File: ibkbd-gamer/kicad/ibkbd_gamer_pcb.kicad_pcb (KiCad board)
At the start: 2 copper layers, 165.6 x 144.3 mm, 35 parts

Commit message: update pcb
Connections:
- S1 pad : P5 -> P2
- S1 pad 1: P5 -> P2
- S10 pad : P7 -> ring_home
- S10 pad 1: P7 -> P4
- S10 pad 2: P16 -> P14
- S11 pad : P7 -> ring_top
- S11 pad 1: P7 -> P4
- S11 pad 2: P18 -> P16
- S12 pad : P7 -> ring_num
- S12 pad 1: P7 -> P4
- S12 pad 2: P19 -> P10
- S13 pad : P8 -> middle_bottom
- S13 pad 1: P8 -> P5
- S14 pad : P8 -> middle_home
- S14 pad 1: P8 -> P5
- S14 pad 2: P16 -> P14
- S15 pad : P8 -> middle_top
- S15 pad 1: P8 -> P5
- S15 pad 2: P18 -> P16
- S16 pad : P8 -> middle_num
- S16 pad 1: P8 -> P5
- S16 pad 2: P19 -> P10
- S17 pad : P9 -> index_bottom
- S17 pad 1: P9 -> P6
- S18 pad : P9 -> index_home
- S18 pad 1: P9 -> P6
- S18 pad 2: P16 -> P14
- S19 pad : P9 -> index_top
- S19 pad 1: P9 -> P6
- S19 pad 2: P18 -> P16
- S2 pad : P5 -> outer_home
- S2 pad 1: P5 -> P2
- S2 pad 2: P16 -> P14
- S20 pad : P9 -> P6
- S20 pad 1: P9 -> P6
- S20 pad 2: P19 -> P10
- S21 pad : P10 -> inner_bottom
- S21 pad 1: P10 -> P7
- S22 pad : P10 -> inner_home
- S22 pad 1: P10 -> P7
- S22 pad 2: P16 -> P14
- S23 pad : P10 -> inner_top
- S23 pad 1: P10 -> P7
- S23 pad 2: P18 -> P16
- S24 pad : P10 -> P7
- S24 pad 1: P10 -> P7
- S24 pad 2: P19 -> P10
- S25 pad : P14 -> extra_home
- S25 pad 1: P14 -> P8
- S25 pad 2: P16 -> P14
- S26 pad : P14 -> extra_top
- S26 pad 1: P14 -> P8
- S26 pad 2: P18 -> P16
- S27 pad : P14 -> extra_num
- S27 pad 1: P14 -> P8
- S27 pad 2: P19 -> P10
- S28 pad : P9 -> P6
- S28 pad 1: P9 -> P6
- S28 pad 2: P20 -> P18
- S29 pad : P10 -> home_thumb
- S29 pad 1: P10 -> P7
- S29 pad 2: P20 -> P18
- S3 pad : P5 -> outer_top
- S3 pad 1: P5 -> P2
- S3 pad 2: P18 -> P16
- S30 pad : P10 -> far_thumb
- S30 pad 1: P10 -> P7
- S30 pad 2: P21 -> P19
- S31 pad : P14 -> gk1_thumb
- S31 pad 1: P14 -> P8
- S31 pad 2: P20 -> P18
- S32 pad : P14 -> gk2_thumb
- S32 pad 1: P14 -> P8
- S33 pad : P14 -> P8
- S33 pad 1: P14 -> P8
- S33 pad 2: P21 -> P19
- S4 pad : P5 -> outer_num
- S4 pad 1: P5 -> P2
- S4 pad 2: P19 -> P10
- S5 pad : P6 -> P3
- S5 pad 1: P6 -> P3
- S6 pad : P6 -> pinky_home
- S6 pad 1: P6 -> P3
- S6 pad 2: P16 -> P14
- S7 pad : P6 -> P3
- S7 pad 1: P6 -> P3
- S7 pad 2: P18 -> P16
- S8 pad : P6 -> P3
- S8 pad 1: P6 -> P3
- S8 pad 2: P19 -> P10
- S9 pad : P7 -> ring_bottom
- S9 pad 1: P7 -> P4
- TRRS1 pad 3: P4 -> P9
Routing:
- net P19: track 0.00 -> 272.1 mm
- net P8: track 63.2 -> 328.2 mm
- net (no net): track 262.1 -> 0.00 mm
- net P18: track 0.00 -> 254.6 mm
- net P15: track 0.00 -> 250.1 mm
- net P7: track 63.2 -> 306.6 mm
- net P16: track 0.00 -> 194.4 mm
- net P6: track 63.2 -> 247.4 mm
- net GND: track 0.00 -> 169.9 mm
- net P4: track 0.00 -> 168.2 mm
- net P3: track 0.00 -> 154.6 mm
- net P2: track 0.00 -> 147.1 mm
- net VCC: track 0.00 -> 135.6 mm
- net P14: track 94.9 -> 228.2 mm
- net P5: track 63.2 -> 187.3 mm
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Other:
- net class Default removed

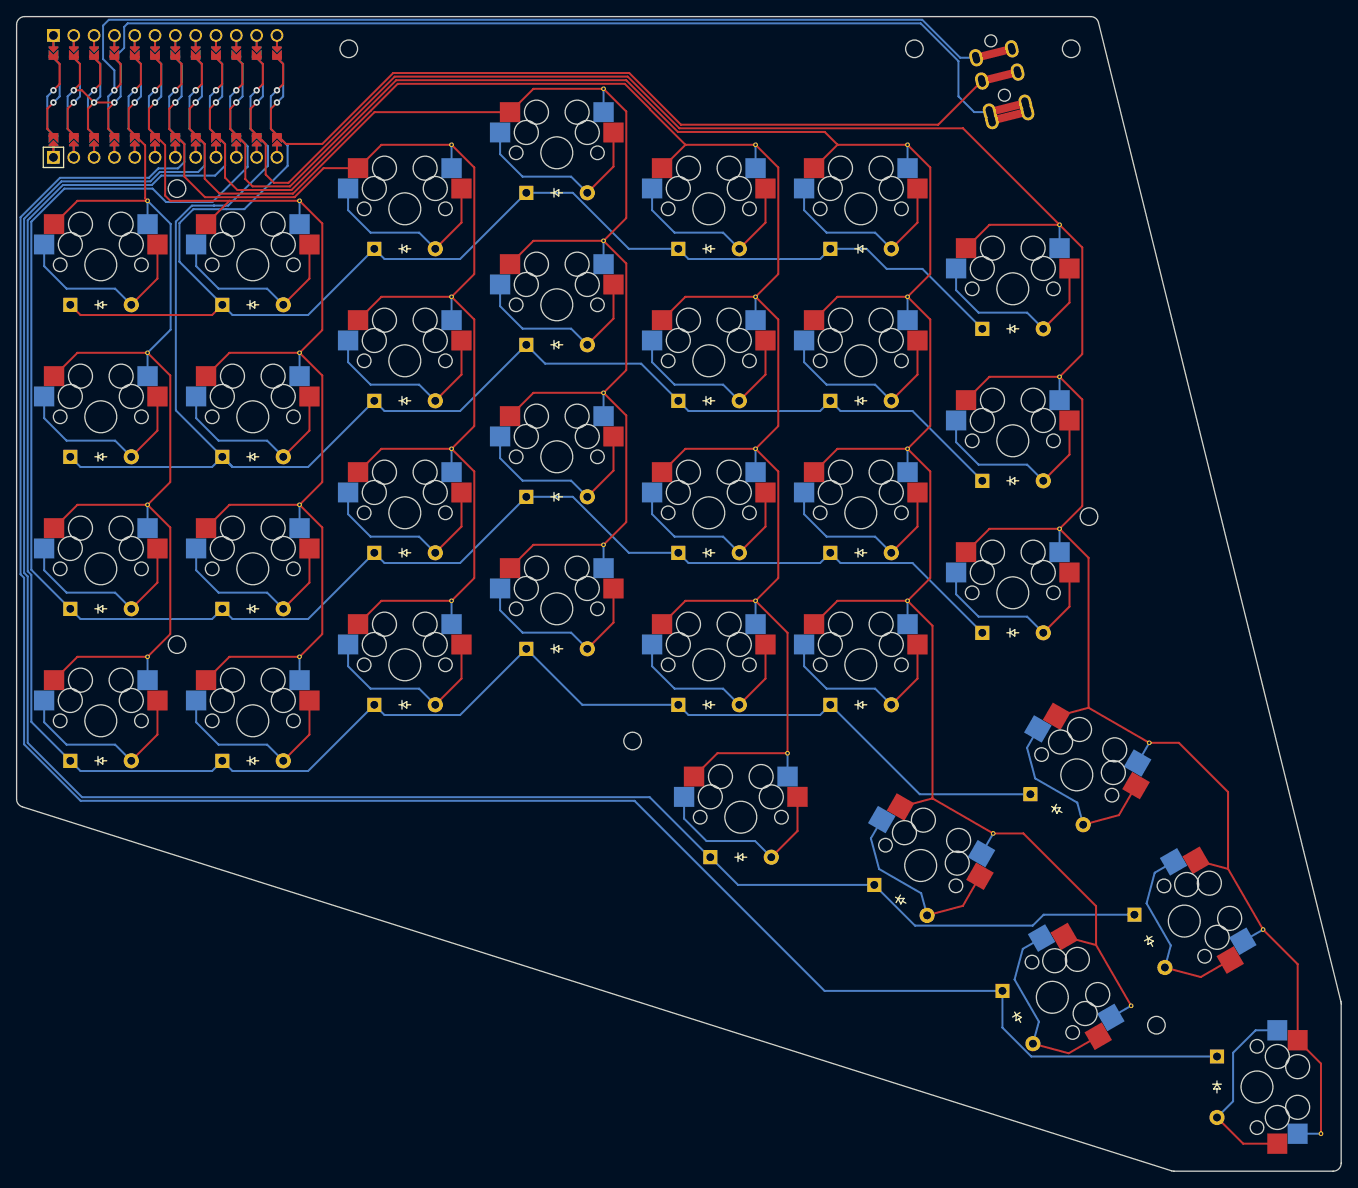
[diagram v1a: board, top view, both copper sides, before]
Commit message: move to through hole design
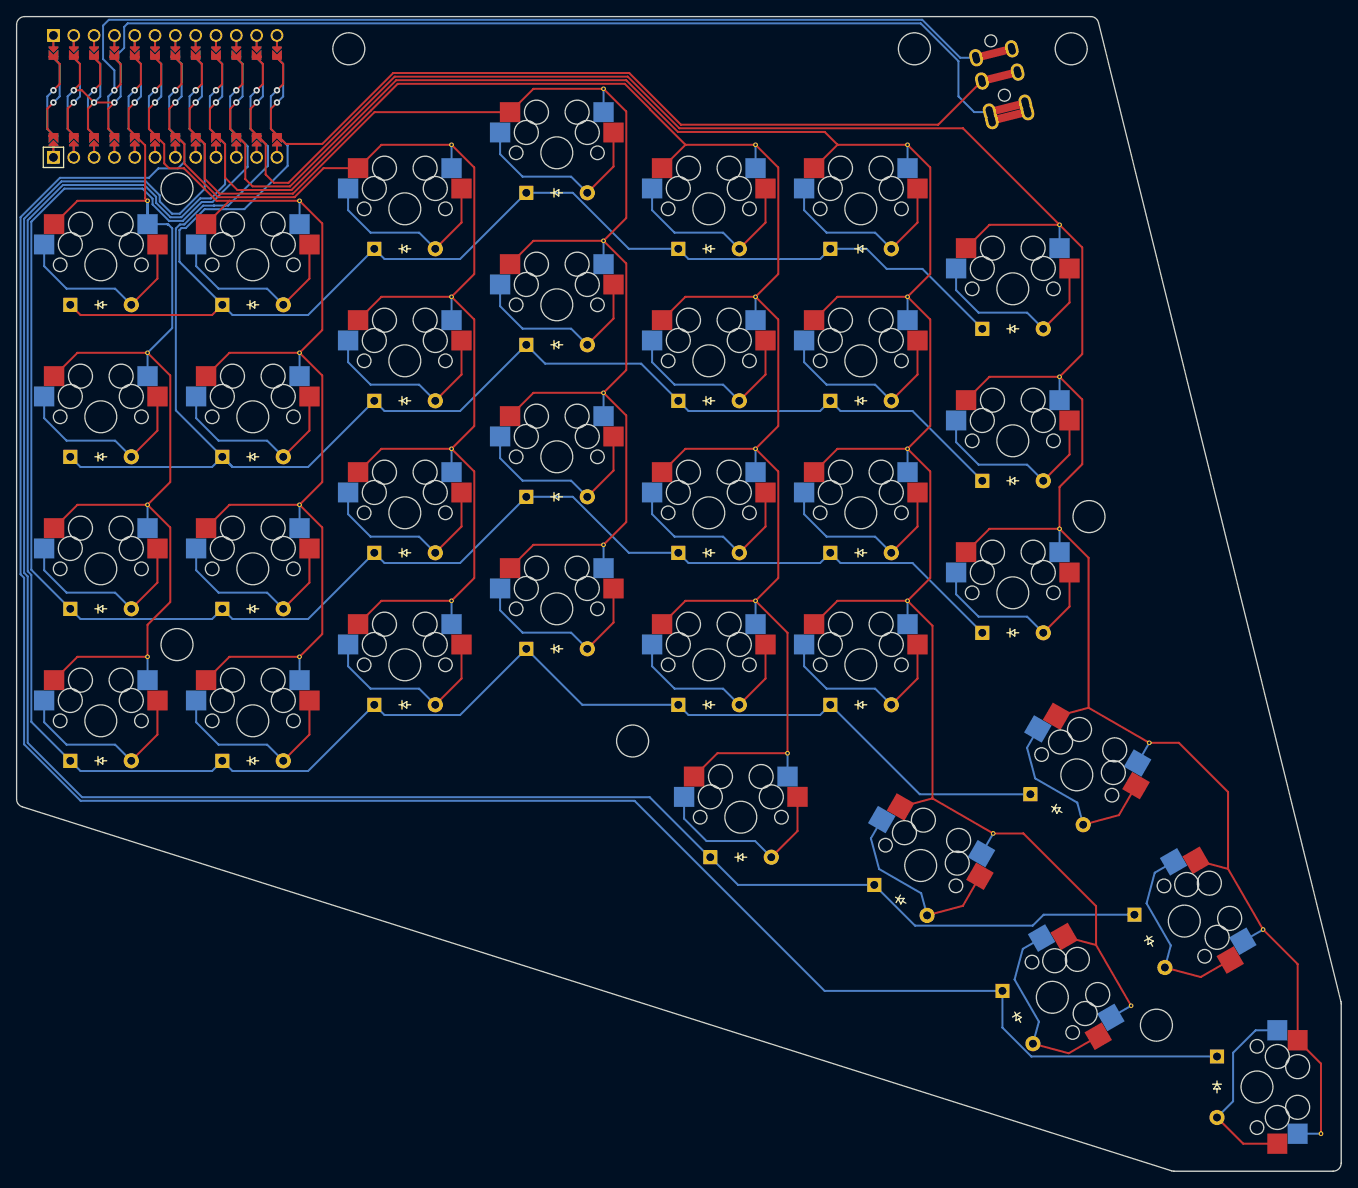
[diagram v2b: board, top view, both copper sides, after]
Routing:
- net P18: track 254.6 -> 260.1 mm
- net P15: track 250.1 -> 255.2 mm
- net P14: track 228.2 -> 230.6 mm
- net P3: track 154.6 -> 152.3 mm
- net P2: track 147.1 -> 148.8 mm
- net P4: track 168.2 -> 167.2 mm
- net P16: track 194.4 -> 193.9 mm
- net P10: track 175.3 -> 174.8 mm
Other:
- outline, holes or cut-outs redrawn
